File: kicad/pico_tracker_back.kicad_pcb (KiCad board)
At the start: 2 copper layers, 92.9 x 125.4 mm, 2 parts

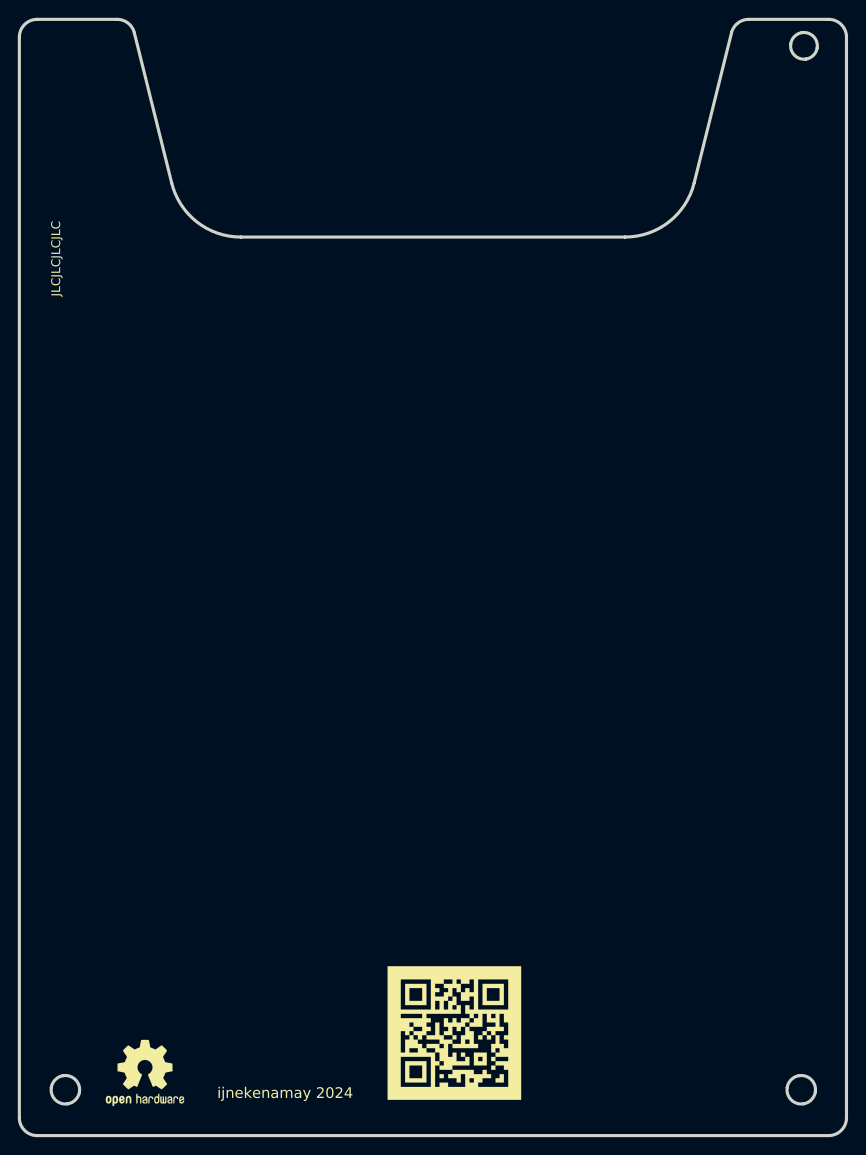
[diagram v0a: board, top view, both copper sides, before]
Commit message: fix alignment holes
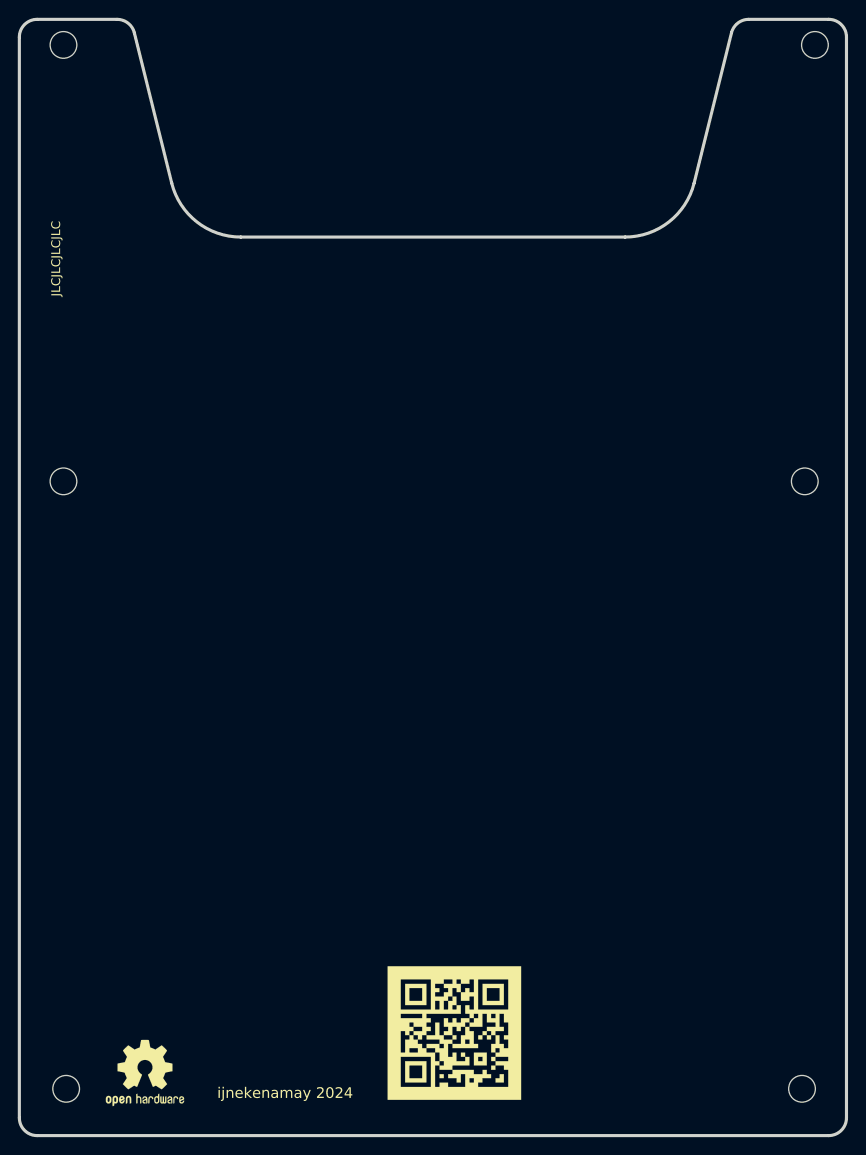
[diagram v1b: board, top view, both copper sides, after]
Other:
- outline, holes or cut-outs redrawn
